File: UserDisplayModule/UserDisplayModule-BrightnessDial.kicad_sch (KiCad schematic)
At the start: 5 parts, among them U2 LM324

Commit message: doubled LEDs + started PCB
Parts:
- C1: value C -> 10µ; footprint (none) -> Capacitor_SMD:C_0805_2012Metric
- R22: value R_US -> 16k; footprint (none) -> Resistor_SMD:R_0805_2012Metric
- RV1: footprint (none) -> Potentiometer_THT:Potentiometer_Rotary
- U2: footprint (none) -> ImportedFootprints:LM324N
- renumbered D22 to D41
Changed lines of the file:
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@@
 			)
 		)
-		(property "Footprint" ""
+		(property "Footprint" "ImportedFootprints:LM324N"
 			(at 30.48 33.02 0)
 			(effects
@@
 			)
 		)
-		(property "Footprint" ""
+		(property "Footprint" "Potentiometer_THT:Potentiometer_Rotary"
 			(at 41.91 34.29 0)
 			(effects
@@
 		(on_board yes)
 		(dnp no)
-		(fields_autoplaced yes)
 		(property "Reference" "C1"
-			(at 88.9 39.3699 0)
+			(at 88.138 39.37 0)
 			(effects
 				(font
@@
 			)
 		)
-		(property "Value" "C"
-			(at 88.9 41.9099 0)
+		(property "Value" "10µ"
+			(at 88.138 41.91 0)
 			(effects
 				(font
@@
 			)
 		)
-		(property "Footprint" ""
+		(property "Footprint" "Capacitor_SMD:C_0805_2012Metric"
 			(at 86.0552 44.45 0)
 			(effects
@@
 			)
 		)
-		(property "Footprint" ""
+		(property "Footprint" "ImportedFootprints:LM324N"
 			(at 101.6 36.83 0)
 			(effects
@@
 			)
 		)
-		(property "Footprint" ""
+		(property "Footprint" "ImportedFootprints:LM324N"
 			(at 60.96 34.29 0)
 			(effects
@@
 		(on_board yes)
 		(dnp no)
-		(property "Reference" "D22"
+		(property "Reference" "D41"
 			(at 46.228 44.704 90)
 			(effects
@@
 			(project "UserDisplayModule"
 				(path "/352d7abe-fc72-4473-8b68-62eecf44f496/ed6b1e35-5147-4efc-b415-ad1fa40d2595"
-					(reference "D22")
+					(reference "D41")
 					(unit 1)
 				)
@@
 			)
 		)
-		(property "Value" "R_US"
+		(property "Value" "16k"
 			(at 78.74 33.02 90)
 			(effects
@@
 			)
 		)
-		(property "Footprint" ""
+		(property "Footprint" "Resistor_SMD:R_0805_2012Metric"
 			(at 78.994 35.814 90)
 			(effects

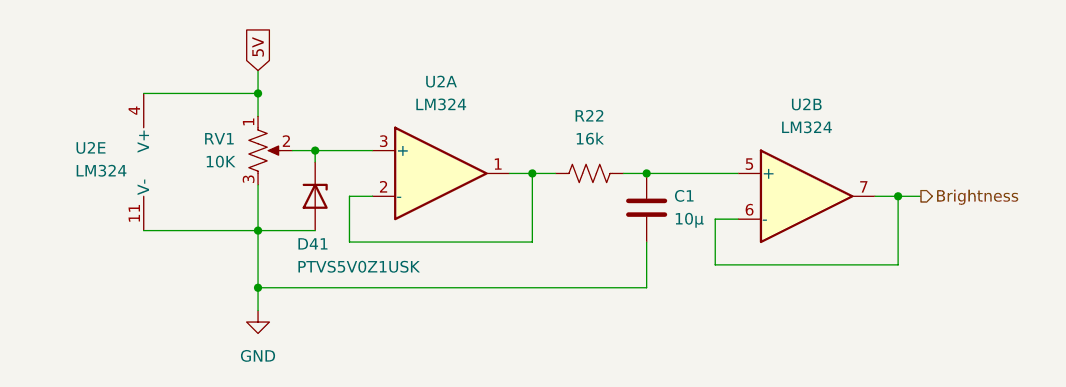
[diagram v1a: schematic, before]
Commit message: finished routing pcb (minus ground pour)
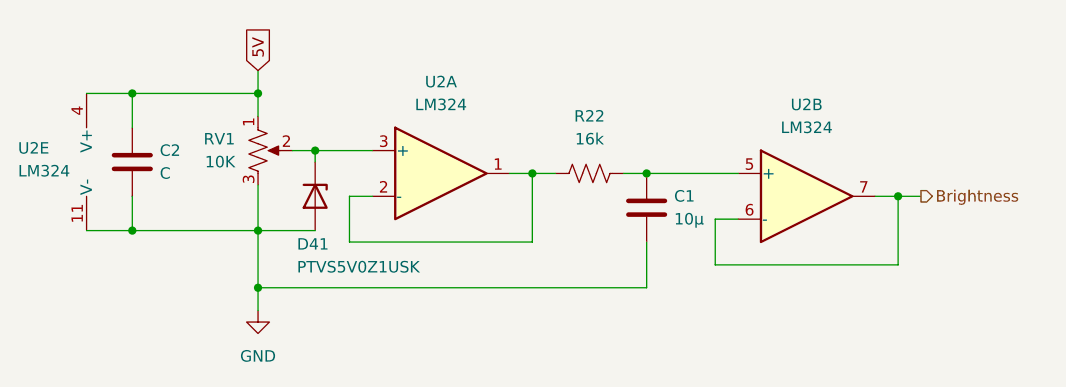
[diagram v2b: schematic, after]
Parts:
- added C2: C, Capacitor_SMD:C_0805_2012Metric, symbol Device:C
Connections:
- net 5V: now also C2.1
- net GND: now also C2.2
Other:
- moved on the sheet: U2E
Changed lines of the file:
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@@
+	)
+	(junction
+		(at 27.94 43.18)
+		(diameter 0)
+		(color 0 0 0 0)
+	)
+	(junction
+		(at 27.94 27.94)
+		(diameter 0)
+		(color 0 0 0 0)
 	)
 	(junction
@@
 	(wire
 		(pts
-			(xy 29.21 43.18) (xy 41.91 43.18)
+			(xy 22.86 43.18) (xy 27.94 43.18)
 		)
 		(stroke
@@
 	(wire
 		(pts
+			(xy 27.94 43.18) (xy 41.91 43.18)
+		)
+		(stroke
+			(width 0)
+			(type default)
+		)
+	)
+	(wire
+		(pts
 			(xy 82.55 36.83) (xy 85.09 36.83)
 		)
@@
 	(wire
 		(pts
+			(xy 27.94 27.94) (xy 41.91 27.94)
+		)
+		(stroke
+			(width 0)
+			(type default)
+		)
+	)
+	(wire
+		(pts
 			(xy 72.39 36.83) (xy 74.93 36.83)
 		)
@@
 	(wire
 		(pts
+			(xy 27.94 39.37) (xy 27.94 43.18)
+		)
+		(stroke
+			(width 0)
+			(type default)
+		)
+	)
+	(wire
+		(pts
+			(xy 27.94 27.94) (xy 27.94 31.75)
+		)
+		(stroke
+			(width 0)
+			(type default)
+		)
+	)
+	(wire
+		(pts
 			(xy 41.91 52.07) (xy 41.91 49.53)
 		)
@@
 	(wire
 		(pts
-			(xy 29.21 27.94) (xy 41.91 27.94)
+			(xy 22.86 27.94) (xy 27.94 27.94)
 		)
 		(stroke
@@
 	(symbol
 		(lib_id "Amplifier_Operational:LM324")
-		(at 31.75 35.56 0)
+		(at 25.4 35.56 0)
 		(unit 5)
 		(exclude_from_sim no)
@@
 		(dnp no)
 		(property "Reference" "U2"
-			(at 21.59 34.036 0)
+			(at 15.24 34.036 0)
 			(effects
 				(font
@@
 		)
 		(property "Value" "LM324"
-			(at 21.59 36.576 0)
+			(at 15.24 36.576 0)
 			(effects
 				(font
@@
 		)
 		(property "Footprint" "ImportedFootprints:LM324N"
-			(at 30.48 33.02 0)
+			(at 24.13 33.02 0)
 			(effects
 				(font
@@
 		)
 		(property "Datasheet" "http://www.ti.com/lit/ds/symlink/lm2902-n.pdf"
-			(at 33.02 30.48 0)
+			(at 26.67 30.48 0)
 			(effects
 				(font
@@
 		)
 		(property "Description" "Low-Power, Quad-Operational Amplifiers, DIP-14/SOIC-14/SSOP-14"
-			(at 31.75 35.56 0)
+			(at 25.4 35.56 0)
 			(effects
 				(font
@@
 					(unit 1)
 				)
+			)
+		)
+	)
+	(symbol
+		(lib_id "Device:C")
+		(at 27.94 35.56 0)
+		(unit 1)
+		(exclude_from_sim no)
+		(in_bom yes)
+		(on_board yes)
+		(dnp no)
+		(property "Reference" "C2"
+			(at 30.988 34.29 0)
+			(effects
+				(font
+					(size 1.27 1.27)
+				)
+				(justify left)
+			)
+		)
+		(property "Value" "C"
+			(at 30.988 36.83 0)
+			(effects
+				(font
+					(size 1.27 1.27)
+				)
+				(justify left)
+			)
+		)
+		(property "Footprint" "Capacitor_SMD:C_0805_2012Metric"
+			(at 28.9052 39.37 0)
+			(effects
+				(font
+					(size 1.27 1.27)
+				)
+				(hide yes)
+			)
+		)
+		(property "Datasheet" "~"
+			(at 27.94 35.56 0)
+			(effects
+				(font
+					(size 1.27 1.27)
+				)
+				(hide yes)
+			)
+		)
+		(property "Description" "Unpolarized capacitor"
+			(at 27.94 35.56 0)
+			(effects
+				(font
+					(size 1.27 1.27)
+				)
+				(hide yes)
+			)
+		)
+		(pin "2"
+		)
+		(pin "1"
+		)
+		(instances
+			(project "UserDisplayModule"
+				(path "/352d7abe-fc72-4473-8b68-62eecf44f496/ed6b1e35-5147-4efc-b415-ad1fa40d2595"
+					(reference "C2")
+					(unit 1)
+				)

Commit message: added 3d models, fixed footprints, finished routing
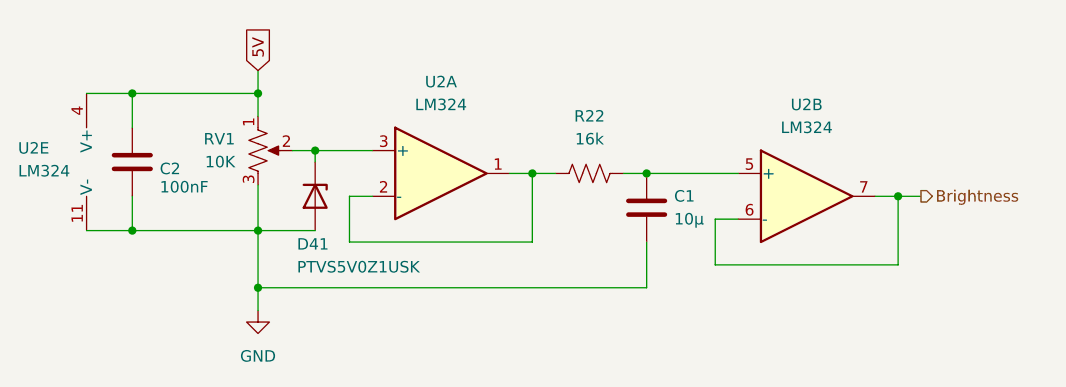
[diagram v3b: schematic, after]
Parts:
- C2: value C -> 100nF
- RV1: footprint Potentiometer_THT:Potentiometer_Rotary -> Potentiometer_THT:Potentiometer_TT_P0915N
- U2: footprint ImportedFootprints:LM324N -> Package_DIP:DIP-14_W7.62mm
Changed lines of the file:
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@@
 			)
 		)
-		(property "Footprint" "ImportedFootprints:LM324N"
+		(property "Footprint" "Package_DIP:DIP-14_W7.62mm"
 			(at 24.13 33.02 0)
 			(effects
@@
 			)
 		)
-		(property "Footprint" "Potentiometer_THT:Potentiometer_Rotary"
+		(property "Footprint" "Potentiometer_THT:Potentiometer_TT_P0915N"
 			(at 41.91 34.29 0)
 			(effects
@@
 		(dnp no)
 		(property "Reference" "C2"
-			(at 30.988 34.29 0)
+			(at 30.988 36.322 0)
 			(effects
 				(font
@@
 			)
 		)
-		(property "Value" "C"
-			(at 30.988 36.83 0)
+		(property "Value" "100nF"
+			(at 30.988 38.354 0)
 			(effects
 				(font
@@
 			)
 		)
-		(property "Footprint" "ImportedFootprints:LM324N"
+		(property "Footprint" "Package_DIP:DIP-14_W7.62mm"
 			(at 101.6 36.83 0)
 			(effects
@@
 			)
 		)
-		(property "Footprint" "ImportedFootprints:LM324N"
+		(property "Footprint" "Package_DIP:DIP-14_W7.62mm"
 			(at 60.96 34.29 0)
 			(effects

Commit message: added digikey pns
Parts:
- U2: Digikey PN (none) -> 296-1391-5-ND
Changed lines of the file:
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@@
 	(generator_version "8.0")
 	(paper "A4")
+	(title_block
+		(date "2024-04-01")
+		(rev "1")
+	)
 	(junction
 		(at 41.91 27.94)
@@
 		)
 		(property "Description" "Low-Power, Quad-Operational Amplifiers, DIP-14/SOIC-14/SSOP-14"
+			(at 25.4 35.56 0)
+			(effects
+				(font
+					(size 1.27 1.27)
+				)
+				(hide yes)
+			)
+		)
+		(property "Digikey PN" "296-1391-5-ND"
 			(at 25.4 35.56 0)
 			(effects
@@
 			)
 		)
+		(property "Digikey PN" ""
+			(at 41.91 34.29 0)
+			(effects
+				(font
+					(size 1.27 1.27)
+				)
+				(hide yes)
+			)
+		)
 		(pin "3"
 		)
@@
 			)
 		)
+		(property "Digikey PN" ""
+			(at 85.09 40.64 0)
+			(effects
+				(font
+					(size 1.27 1.27)
+				)
+				(hide yes)
+			)
+		)
 		(pin "1"
 		)
@@
 		)
 		(property "Description" "Unpolarized capacitor"
+			(at 27.94 35.56 0)
+			(effects
+				(font
+					(size 1.27 1.27)
+				)
+				(hide yes)
+			)
+		)
+		(property "Digikey PN" ""
 			(at 27.94 35.56 0)
 			(effects
@@
 			)
 		)
+		(property "Digikey PN" "296-1391-5-ND"
+			(at 102.87 39.37 0)
+			(effects
+				(font
+					(size 1.27 1.27)
+				)
+				(hide yes)
+			)
+		)
 		(pin "9"
 		)
@@
 			)
 		)
+		(property "Digikey PN" "296-1391-5-ND"
+			(at 62.23 36.83 0)
+			(effects
+				(font
+					(size 1.27 1.27)
+				)
+				(hide yes)
+			)
+		)
 		(pin "2"
 		)
@@
 		)
 		(property "Description" "5V, 1200W TVS unidirectional diode, DSN1608-2"
+			(at 48.26 39.37 0)
+			(effects
+				(font
+					(size 1.27 1.27)
+				)
+				(hide yes)
+			)
+		)
+		(property "Digikey PN" ""
 			(at 48.26 39.37 0)
 			(effects
@@
 			(at 78.74 36.83 0)
 			(effects
+				(font
+					(size 1.27 1.27)
+				)
+				(hide yes)
+			)
+		)
+		(property "Digikey PN" ""
+			(at 78.74 36.83 0)
+			(effects

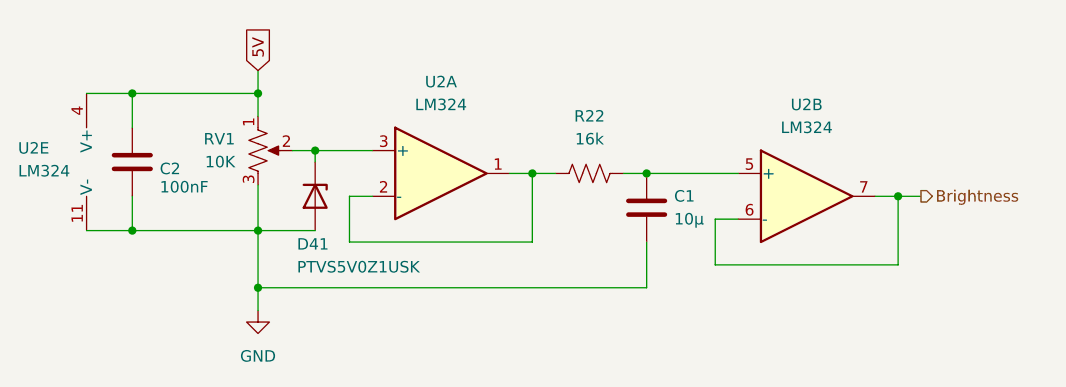
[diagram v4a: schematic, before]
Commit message: Edited BOM for R/C parts
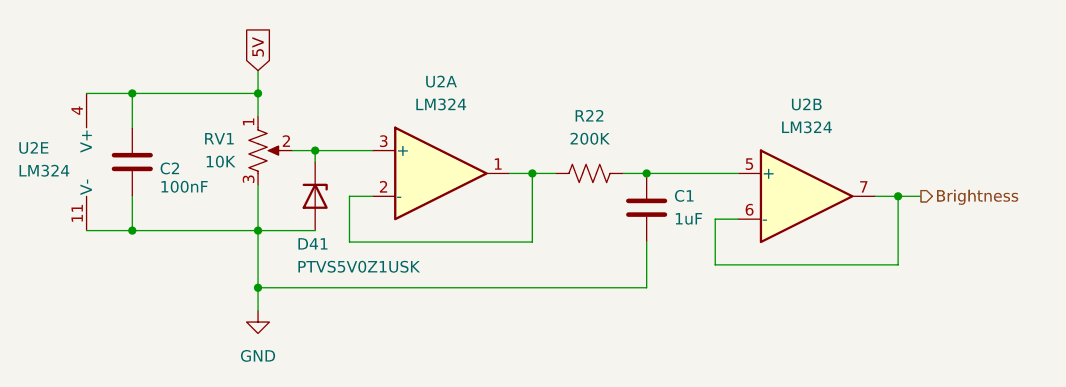
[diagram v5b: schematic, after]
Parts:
- C1: value 10µ -> 1uF; Digikey PN (none) -> 1276-1029-1-ND
- C2: Digikey PN (none) -> 1276-1003-1-ND
- R22: value 16k -> 200K; Digikey PN (none) -> RMCF0805FT200KCT-ND
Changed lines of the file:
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@@
 			)
 		)
-		(property "Value" "10µ"
+		(property "Value" "1uF"
 			(at 88.138 41.91 0)
 			(effects
@@
 			)
 		)
-		(property "Digikey PN" ""
+		(property "Digikey PN" "1276-1029-1-ND"
 			(at 85.09 40.64 0)
 			(effects
@@
 			)
 		)
-		(property "Digikey PN" ""
+		(property "Digikey PN" "1276-1003-1-ND"
 			(at 27.94 35.56 0)
 			(effects
@@
 			)
 		)
-		(property "Value" "16k"
+		(property "Value" "200K"
 			(at 78.74 33.02 90)
 			(effects
@@
 			)
 		)
-		(property "Digikey PN" ""
+		(property "Digikey PN" "RMCF0805FT200KCT-ND"
 			(at 78.74 36.83 0)
 			(effects

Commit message: added digikey PNs to diode and pot
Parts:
- D41: Digikey PN (none) -> 1727-2742-1-ND
- RV1: Digikey PN (none) -> 987-1649-ND
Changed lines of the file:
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@@
 			)
 		)
-		(property "Datasheet" "~"
+		(property "Datasheet" "https://www.ttelectronics.com/TTElectronics/media/ProductFiles/Datasheet/P09x.pdf"
 			(at 41.91 34.29 0)
 			(effects
@@
 			)
 		)
-		(property "Digikey PN" ""
+		(property "Digikey PN" "987-1649-ND"
 			(at 41.91 34.29 0)
 			(effects
@@
 			)
 		)
-		(property "Digikey PN" ""
+		(property "Digikey PN" "1727-2742-1-ND"
 			(at 48.26 39.37 0)
 			(effects
